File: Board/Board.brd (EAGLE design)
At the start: 53.2 x 84.2 mm, 68 parts, among them IC1 MEGA328, IC2 LM358D, IC4 MCP3426, IC6 MCP4921, IC7 TL431CD, Q1 IRLIZ44N, T1 BC817, U1 CJT1117-3.3-SOT223, U3 MCP9701AT-E/TT, U4 IRLML2502

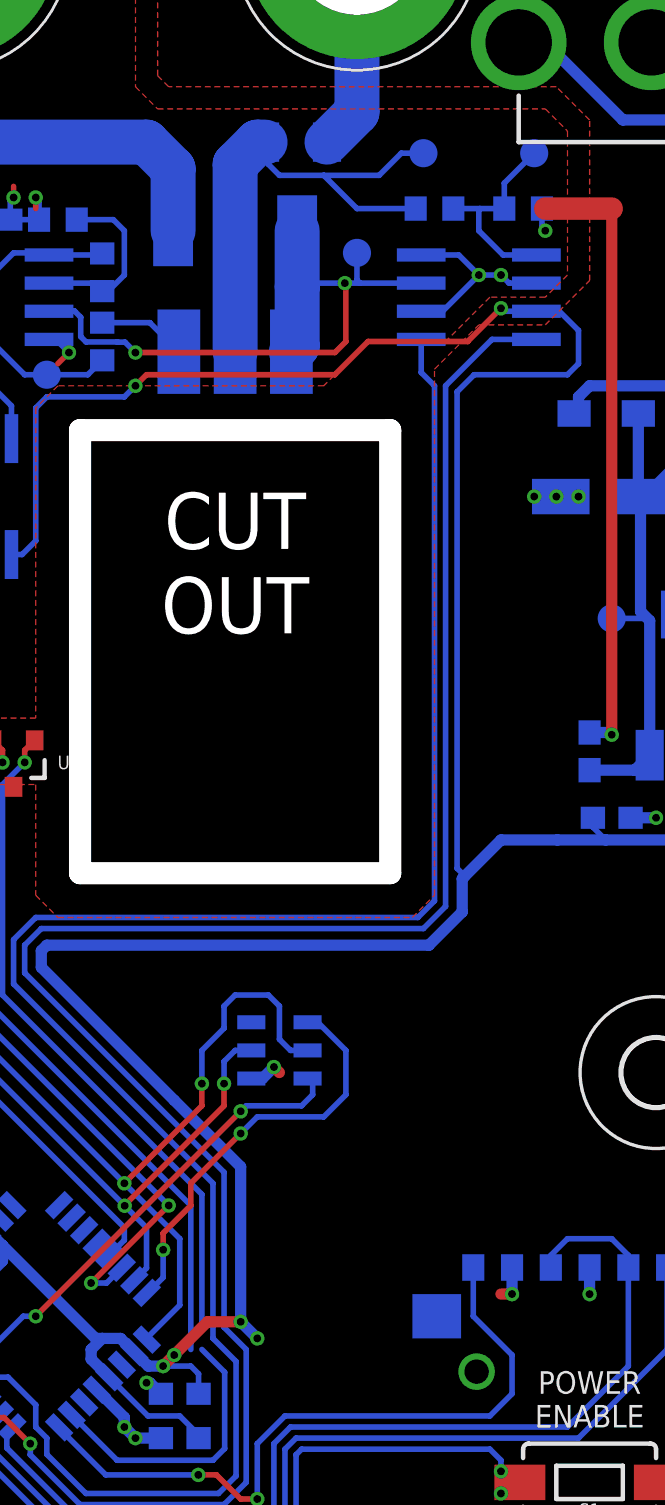
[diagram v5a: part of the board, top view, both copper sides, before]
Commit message: added zener to vload_att net to protect from overvoltage conditions
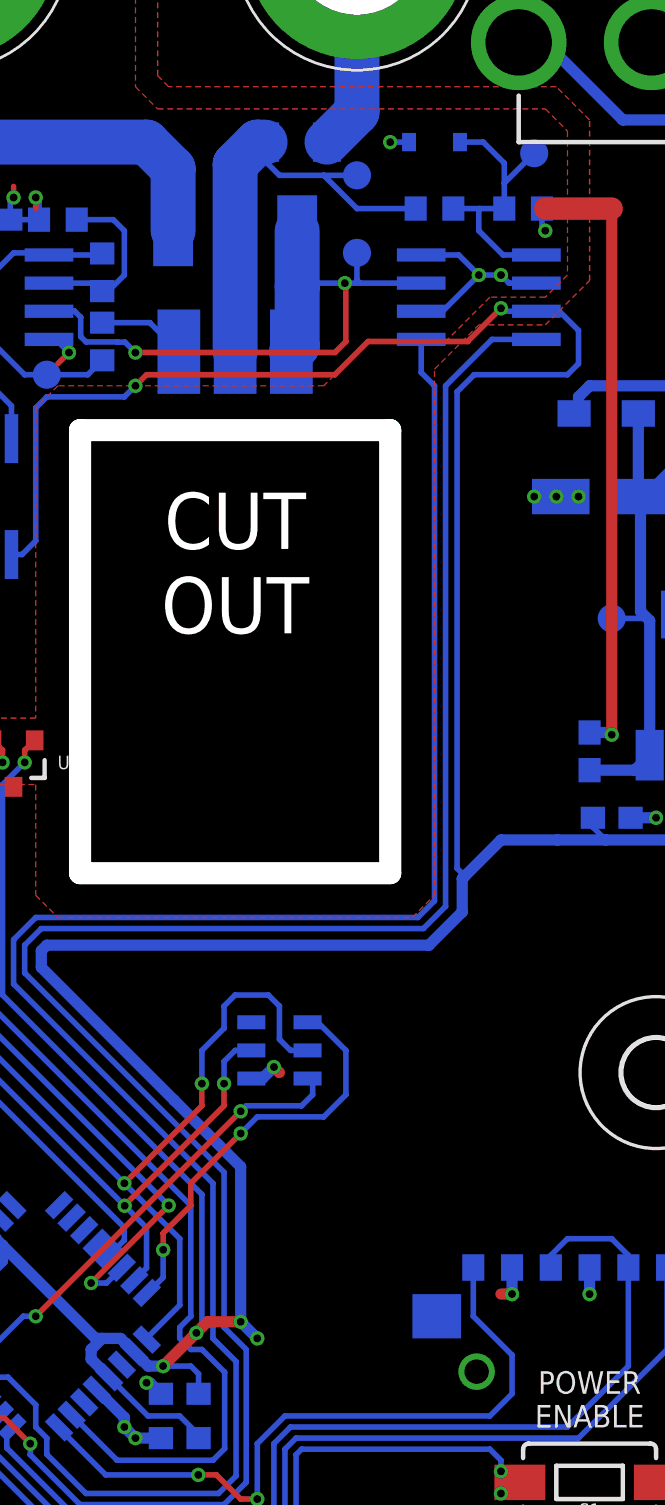
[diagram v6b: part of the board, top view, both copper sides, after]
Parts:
- added D3: 1.1V, SparkFun-DiscreteSemi:SOD-323
- moved ULOAD 3.16 mm to (31.5, 64.5)
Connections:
- net GND: now also D3.A
- net VLOAD_ATT: now also D3.C
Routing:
- net LOAD+: track 23.7 -> 20.3 mm
- net VLOAD_ATT: track 9.58 -> 12.9 mm
- net TEMP: track 44.5 -> 45.4 mm
- net GND: track 115.0 -> 115.8 mm, vias 36 -> 37
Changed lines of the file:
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@@
 <layer number="25" name="tNames" color="7" fill="1" visible="yes" active="yes"/>
 <layer number="26" name="bNames" color="7" fill="1" visible="yes" active="yes"/>
-<layer number="27" name="tValues" color="7" fill="1" visible="yes" active="yes"/>
-<layer number="28" name="bValues" color="7" fill="1" visible="yes" active="yes"/>
+<layer number="27" name="tValues" color="7" fill="1" visible="no" active="yes"/>
+<layer number="28" name="bValues" color="7" fill="1" visible="no" active="yes"/>
 <layer number="29" name="tStop" color="7" fill="3" visible="no" active="yes"/>
 <layer number="30" name="bStop" color="7" fill="6" visible="no" active="yes"/>
@@
 <attribute name="VALUE" x="4.905" y="61.825" size="1.27" layer="28" rot="MR0"/>
 </element>
-<element name="ULOAD" library="testpad" package="B1,27" value="TPB1,27" x="34.5" y="65.5" smashed="yes" rot="MR0">
-<attribute name="NAME" x="34.5" y="66.5" size="0.6096" layer="26" ratio="10" rot="MR0" align="center"/>
-<attribute name="TP_SIGNAL_NAME" value="" x="35.135" y="63.595" size="1" layer="38" rot="MR0"/>
-<attribute name="VALUE" x="35.135" y="64.738" size="0.0254" layer="28" rot="MR0"/>
+<element name="ULOAD" library="testpad" package="B1,27" value="TPB1,27" x="31.5" y="64.5" smashed="yes" rot="MR0">
+<attribute name="NAME" x="31.5" y="65.5" size="0.6096" layer="26" ratio="10" rot="MR0" align="center"/>
+<attribute name="TP_SIGNAL_NAME" value="" x="32.135" y="62.595" size="1" layer="38" rot="MR0"/>
+<attribute name="VALUE" x="32.135" y="63.738" size="0.0254" layer="28" rot="MR0"/>
 </element>
 <element name="UATT" library="testpad" package="B1,27" value="TPB1,27" x="39.5" y="65.5" smashed="yes" rot="MR0">
@@
 <element name="F1" library="Seeed-OPL-fuse" package="F1206" value="6.3A/63V" x="28.75" y="66" rot="MR0"/>
 <element name="U$3" library="SparkFun-Aesthetics" package="OSHW-LOGO-S" value="" x="36.5" y="20.5" rot="MR0"/>
+<element name="D3" library="SparkFun-DiscreteSemi" package="SOD-323" value="1.1V" x="35" y="66" smashed="yes" rot="MR0">
+<attribute name="NAME" x="35" y="67.25" size="0.6096" layer="26" rot="MR0" align="center"/>
+<attribute name="PROD_ID" value="DIO-12442" x="35" y="66" size="1.778" layer="28" rot="MR0" display="off"/>
+<attribute name="VALUE" value="5.6V" x="36.524" y="63.587" size="1.27" layer="28" rot="MR0"/>
+</element>
 </elements>
 <signals>
@@
 <wire x1="11.975" y1="2.5" x2="11.975" y2="2.25" width="0.508" layer="16"/>
 <wire x1="11.975" y1="2.25" x2="11.381915625" y2="1.656915625" width="0.508" layer="16"/>
+<contactref element="D3" pad="A"/>
+<via x="33" y="66" extent="1-16" drill="0.35"/>
+<wire x1="33.85" y1="66" x2="33" y2="66" width="0.254" layer="16"/>
 </signal>
 <signal name="N$1">
@@
 <wire x1="27.5" y1="65.853" x2="27.353" y2="66" width="0.254" layer="16"/>
 <wire x1="31.5" y1="63" x2="30" y2="64.5" width="0.254" layer="16"/>
-<wire x1="30" y1="64.5" x2="32.5" y2="64.5" width="0.254" layer="16"/>
-<wire x1="32.5" y1="64.5" x2="33.5" y2="65.5" width="0.254" layer="16"/>
-<wire x1="33.5" y1="65.5" x2="34.5" y2="65.5" width="0.254" layer="16"/>
+<wire x1="30" y1="64.5" x2="31.5" y2="64.5" width="0.254" layer="16"/>
 </signal>
 <signal name="VLOAD_DROP">
@@
 <wire x1="38.15" y1="63" x2="38.15" y2="64.15" width="0.254" layer="16"/>
 <wire x1="38.15" y1="64.15" x2="39.5" y2="65.5" width="0.254" layer="16"/>
+<contactref element="D3" pad="C"/>
+<wire x1="38.15" y1="65.05" x2="38.15" y2="64.15" width="0.254" layer="16"/>
+<wire x1="36.15" y1="66" x2="37.2" y2="66" width="0.254" layer="16"/>
+<wire x1="37.2" y1="66" x2="38.15" y2="65.05" width="0.254" layer="16"/>
 </signal>
 <signal name="VSW">
@@
 <wire x1="22.75" y1="10.75" x2="22.85" y2="10.75" width="0.508" layer="16"/>
 <wire x1="22.75" y1="10.75" x2="22.078425" y2="10.75" width="0.508" layer="16"/>
-<wire x1="23.25" y1="11.25" x2="22.75" y2="10.75" width="0.254" layer="16"/>
 <wire x1="22.0656875" y1="8.5" x2="20.318171875" y2="10.247515625" width="0.254" layer="16"/>
 <wire x1="22.0656875" y1="8.5" x2="23.5" y2="8.5" width="0.254" layer="16"/>
@@
 <wire x1="23.25" y1="22.75" x2="26.25" y2="19.75" width="0.508" layer="16"/>
 <wire x1="26.25" y1="12.75" x2="24.75" y2="12.75" width="0.508" layer="1"/>
-<wire x1="24.75" y1="12.75" x2="23.25" y2="11.25" width="0.508" layer="1"/>
-<wire x1="23.25" y1="11.25" x2="22.75" y2="10.75" width="0.508" layer="1"/>
+<wire x1="24.75" y1="12.75" x2="24.25" y2="12.25" width="0.508" layer="1"/>
+<wire x1="24.25" y1="12.25" x2="22.75" y2="10.75" width="0.508" layer="1"/>
 <via x="22.75" y="10.75" extent="1-16" drill="0.35"/>
-<via x="23.25" y="11.25" extent="1-16" drill="0.35"/>
+<via x="24.25" y="12.25" extent="1-16" drill="0.35"/>
 <wire x1="23" y1="23" x2="23.25" y2="22.75" width="0.254" layer="16"/>
 <wire x1="24.35" y1="9.5" x2="24.35" y2="10.4" width="0.254" layer="16"/>
@@
 <wire x1="24.5" y1="18.5" x2="24.5" y2="12.5" width="0.254" layer="16"/>
 <wire x1="15.5" y1="27.5" x2="24.5" y2="18.5" width="0.254" layer="16"/>
-<wire x1="24.75" y1="12.75" x2="24.5" y2="12.5" width="0" layer="19" extent="1-16"/>
+<wire x1="24.5" y1="12.5" x2="24.25" y2="12.25" width="0.254" layer="16"/>
 </signal>
 <signal name="DISP_RES">
@@
 <wire x1="15" y1="37.5" x2="15" y2="27" width="0.254" layer="16"/>
 <wire x1="15" y1="27" x2="24" y2="18" width="0.254" layer="16"/>
-<wire x1="24" y1="18" x2="24" y2="11.5" width="0.254" layer="16"/>
-<wire x1="24.5" y1="11.5" x2="24" y2="11.5" width="0" layer="19" extent="16-16"/>
+<wire x1="24" y1="18" x2="24" y2="13" width="0.254" layer="16"/>
+<wire x1="24" y1="13" x2="23.5" y2="12.5" width="0.254" layer="16"/>
+<wire x1="23.5" y1="12.5" x2="23.5" y2="12" width="0.254" layer="16"/>
+<wire x1="23.5" y1="12" x2="24" y2="11.5" width="0.254" layer="16"/>
+<wire x1="24" y1="11.5" x2="24.5" y2="11.5" width="0.254" layer="16"/>
 </signal>
 <signal name="RESET">

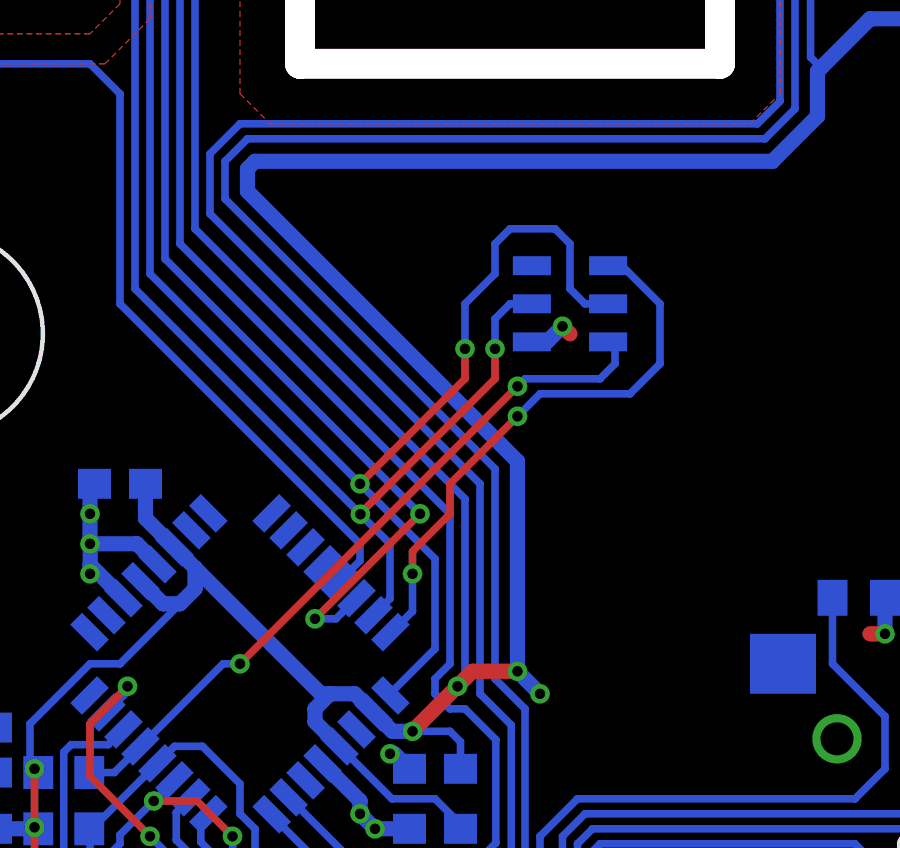
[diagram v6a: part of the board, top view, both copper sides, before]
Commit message: added throughhole ICSP header
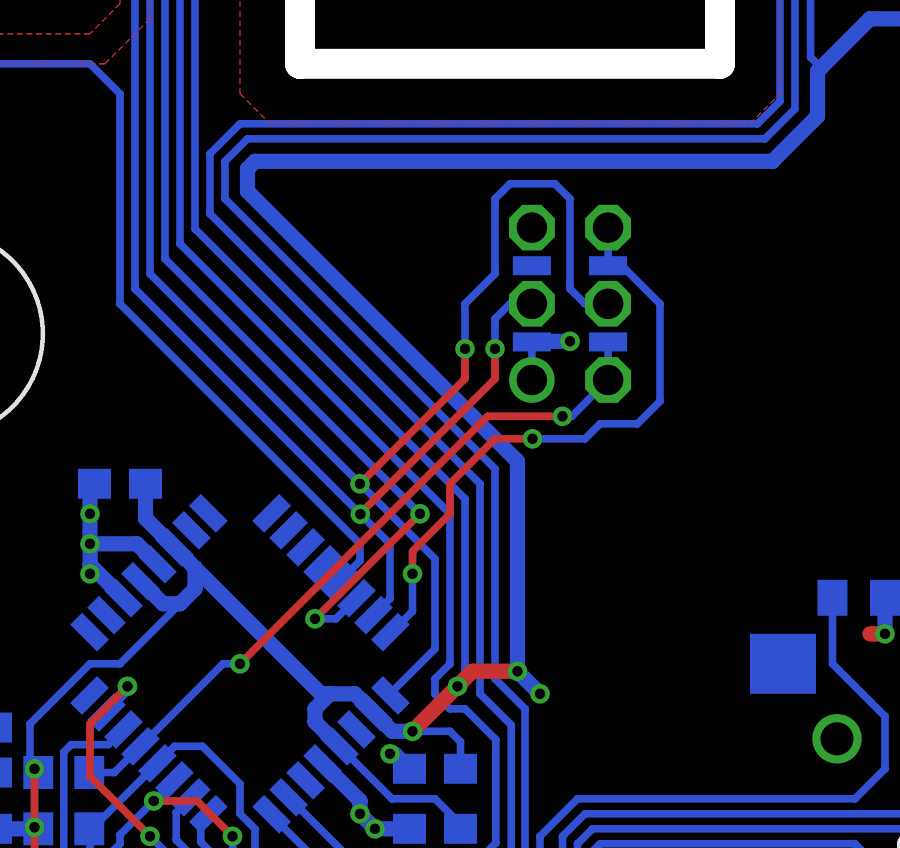
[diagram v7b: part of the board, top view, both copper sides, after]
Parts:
- added SV1: (no value), con-lstb:MA03-2
- U$4: value ICSPSMD -> ICSP; device OwnStuff:ICSP-SMD -> OwnStuff:ICSP-SMD-NOSILK
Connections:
- new net +5V: SV1.5
- net GND: now also SV1.1
- net MISO: now also SV1.6
- net MOSI: now also SV1.3
- net RESET: now also SV1.2
- net SCK: now also SV1.4
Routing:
- net SCK: track 56.3 -> 59.3 mm
- net MISO: track 18.7 -> 20.7 mm
- net GND: track 115.8 -> 116.8 mm
